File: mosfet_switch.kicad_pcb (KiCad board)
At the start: 2 copper layers, 62 parts, among them J1 Conn_01x06_Pin, Q1 IRFS4310Z, Q10 BCX56, Q11 BCX53, Q12 BCX56, Q13 BCX56, Q14 BCX53, Q15 BCX56, Q2 IRFS4310Z, Q3 IRFS4310Z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

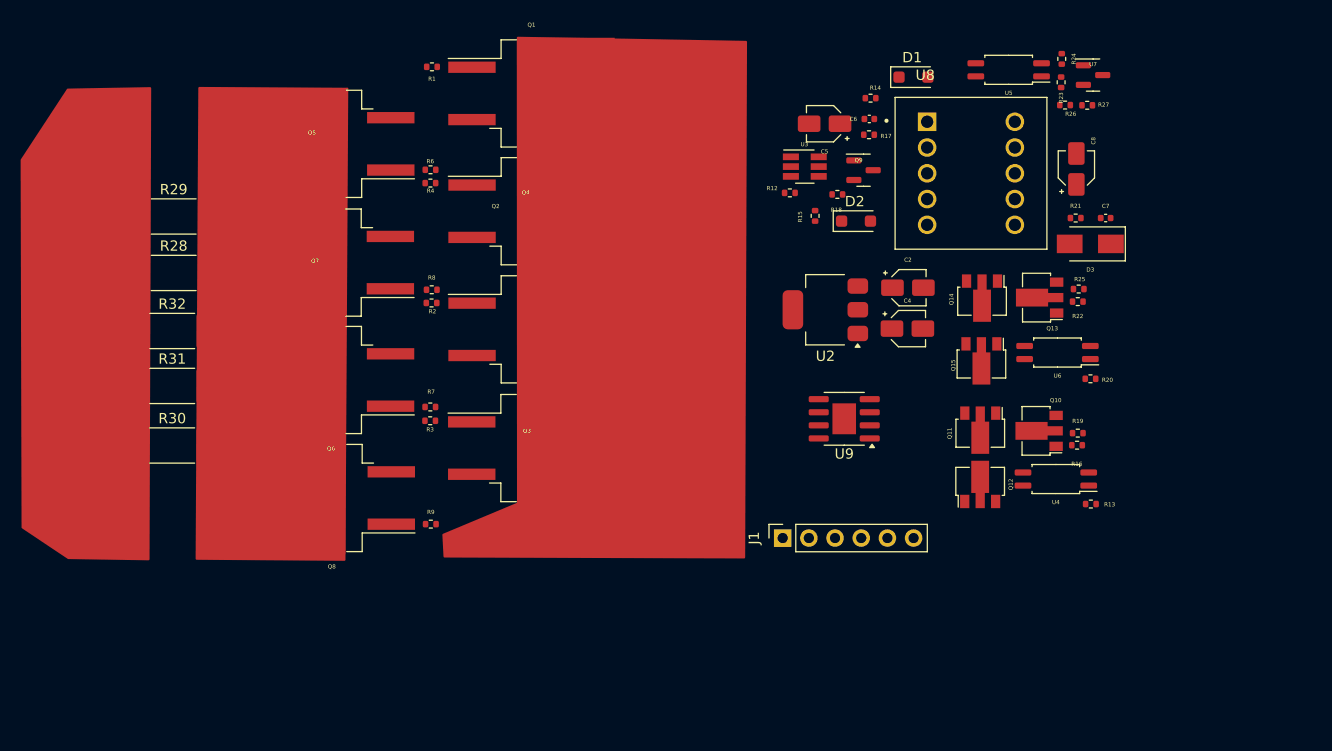
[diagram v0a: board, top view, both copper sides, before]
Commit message: [TL431 Circuit] Pick component value
Work on calculating isolated voltage feed back circuitry
changed smps switch mosfet.
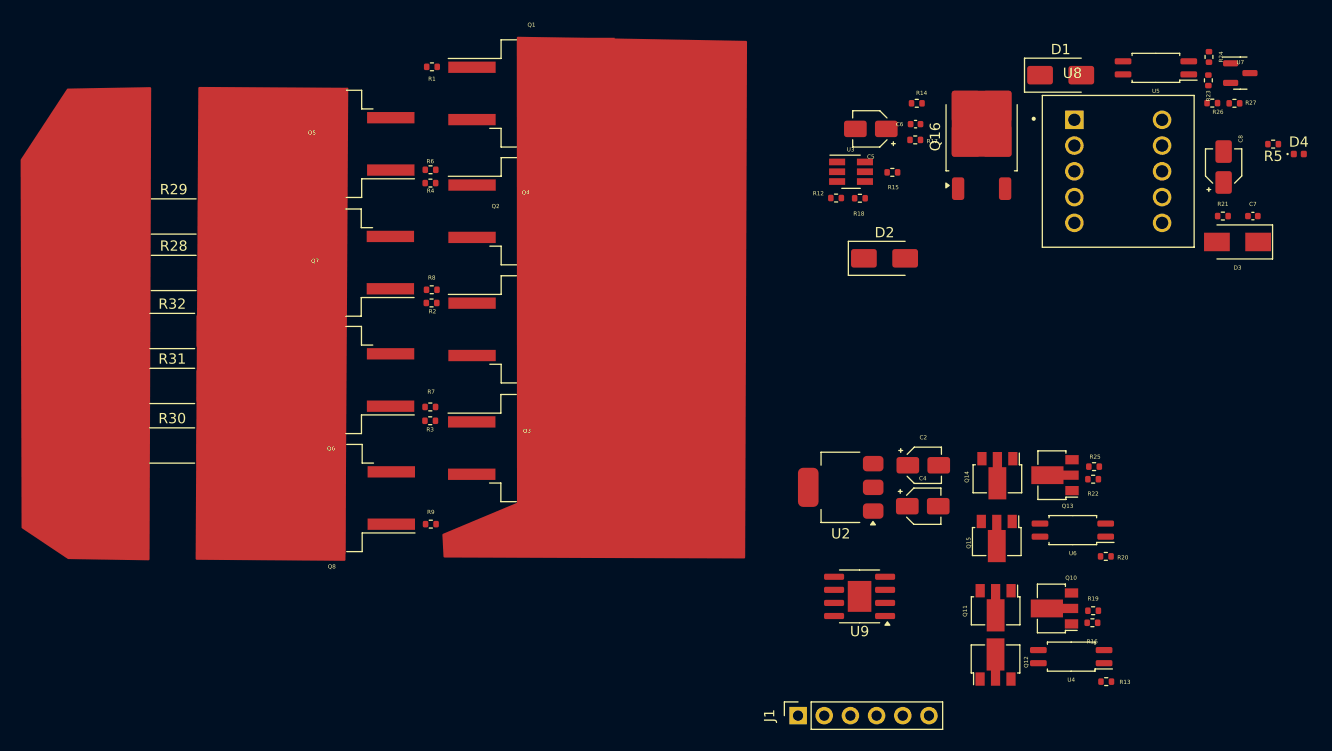
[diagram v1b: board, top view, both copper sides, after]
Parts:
- removed Q9: AO3400A, Package_TO_SOT_SMD:SOT-23
- added D4: LED, LED_SMD:LED_0402_1005Metric, F.Cu at (210.0, 72.6)
- added Q16: IRFR220NTRLPBF, Package_TO_SOT_SMD:TO-252-2, F.Cu at (179.2, 70.9)
- added R5: 330, Resistor_SMD:R_0402_1005Metric, F.Cu at (207.5, 71.6)
- D1, D2: value B160-E3 -> ES1D; footprint Diode_SMD:D_SOD-123F -> Diode_SMD:D_SMA
- D3: value B160-E3 -> ES1D
- R23: value 100R -> 500
- R26: value 100R -> 3.4k
- R27: value 100R -> 900
- moved C2 17.3 mm to (173.6, 102.8)
- moved J1 17.3 mm to (161.4, 127.1)
- moved Q11 17.3 mm to (180.6, 116.6)
- moved Q13 17.3 mm to (186.3, 103.8)
- moved Q14 17.3 mm to (180.8, 103.8)
- moved Q15 17.3 mm to (180.7, 109.9)
- moved R13 17.3 mm to (191.3, 123.8)
- moved R16 17.3 mm to (190.0, 118.1)
- moved R20 17.3 mm to (191.3, 111.6)
- moved R25 17.3 mm to (190.1, 102.9)
- moved U2 17.3 mm to (165.6, 104.9)
- moved Q10 17.3 mm to (186.3, 116.7)
- moved Q12 17.3 mm to (180.6, 121.9)
- moved R22 17.3 mm to (190.0, 104.2)
- moved U6 17.3 mm to (188.1, 109.1)
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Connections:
- R26 pad 2: +bat_boost -> Net-(R23-Pad1)
